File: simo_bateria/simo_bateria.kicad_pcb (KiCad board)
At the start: 2 copper layers, 70 x 163.5 mm, 14 parts, among them J1 BAT_LEVEL, J2 Plugin, SW1 SW_Reed, U1 mod_mt3608, U2 BSS314PEH6327XTSA1

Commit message: revision 3.0. Esquema. PCB con posicionamiento tentativo. Falta ver la posicion definitiva y mas conveniente del switch magnetico
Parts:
- added J3: VBAT IN, simo_bateria:JST_EH_B2B-EH-A_1x02_P2.50mm_Vertical, F.Cu at (160.1, 69.5)
- BT1, BT2: value Battery_Cell -> Bateria; footprint simo_bateria:BatteryHolder_MPD_BH-18650-PC2 -> simo_bateria:BH-18650-PC2_virtual
- R1, R2, R3, SW1: footprint Resistor_THT:R_Axial_DIN0309_L9.0mm_D3.2mm_P25.40mm_Horizontal -> Resistor_THT:R_Axial_DIN0309_L9.0mm_D3.2mm_P15.24mm_Horizontal
- U2: moved to B.Cu
- moved BT1 131.6 mm to (60.5, 61.0), turned to 0 degrees
- moved J1 108.9 mm to (160.9, 76.7)
- moved U1 88.7 mm to (193.1, 64.5)
- moved BT2 49.9 mm to (60.5, 82.5), turned to 0 degrees
- moved R3 45.1 mm to (198.1, 82.0), turned to 180 degrees
- moved H2 40.7 mm to (161.6, 59.5)
- moved H1 40.4 mm to (213.6, 59.5)
- moved U2 31.3 mm to (191.6, 75.5), turned to 180 degrees
- moved SW1 30.1 mm to (183.0, 86.5)
- moved J2 29.1 mm to (212.6, 76.3)
- moved R1 25.9 mm to (175.0, 72.4), turned to -90 degrees
- moved R2 23.2 mm to (170.6, 87.6), turned to 90 degrees
- moved H4 23.2 mm to (161.6, 85.5)
- moved H3 22.7 mm to (213.6, 85.0)
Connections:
- BT1 pad 1: Net-(BT1-Pad1) -> unconnected-(BT1-Pad1)
- BT1 pad 2: Net-(BT1-Pad2) -> unconnected-(BT1-Pad2)
- BT2 pad 1: Net-(BT1-Pad1) -> unconnected-(BT2-Pad1)
- BT2 pad 2: Net-(BT1-Pad2) -> unconnected-(BT2-Pad2)
- J1 pad 1: GND -> Net-(J1-Pad1)
- J2 pad 1: GND -> Net-(J2-Pad1)
- R1 pad 1: Net-(BT1-Pad1) -> Net-(R1-Pad1)
- R2 pad 2: GND -> Net-(J1-Pad1)
- R3 pad 2: Net-(BT1-Pad2) -> Net-(R3-Pad2)
- SW1 pad 1: Net-(BT1-Pad1) -> Net-(R1-Pad1)
- U1 pad 2: Net-(BT1-Pad2) -> Net-(R3-Pad2)
- U1 pad 4: GND -> Net-(J2-Pad1)
- U2 pad 3: Net-(BT1-Pad1) -> Net-(R1-Pad1)
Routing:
- net Net-(R1-Pad1): track 0.00 -> 47.1 mm
- net Net-(R3-Pad2): track 0.00 -> 32.9 mm
- net Net-(J2-Pad2): track 0.00 -> 22.8 mm
- net Net-(U1-Pad1): track 0.00 -> 22.1 mm
- net Net-(J1-Pad2): track 0.00 -> 18.3 mm
- net Net-(R3-Pad1): track 0.00 -> 14.9 mm
- net Net-(J1-Pad1): track 0.00 -> 13.0 mm
- net Net-(J2-Pad1): track 0.00 -> 7.78 mm
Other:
- board size 70 x 163.5 mm -> 65 x 35 mm
- board text added: "Los portabaterias no forman parte del pcb. La tension de entrada ingresa por el conector VBAT IN"
- board text added: "Posicionamiento tentativo. Aun falta definir y probar dorde ira el switch magnetico"

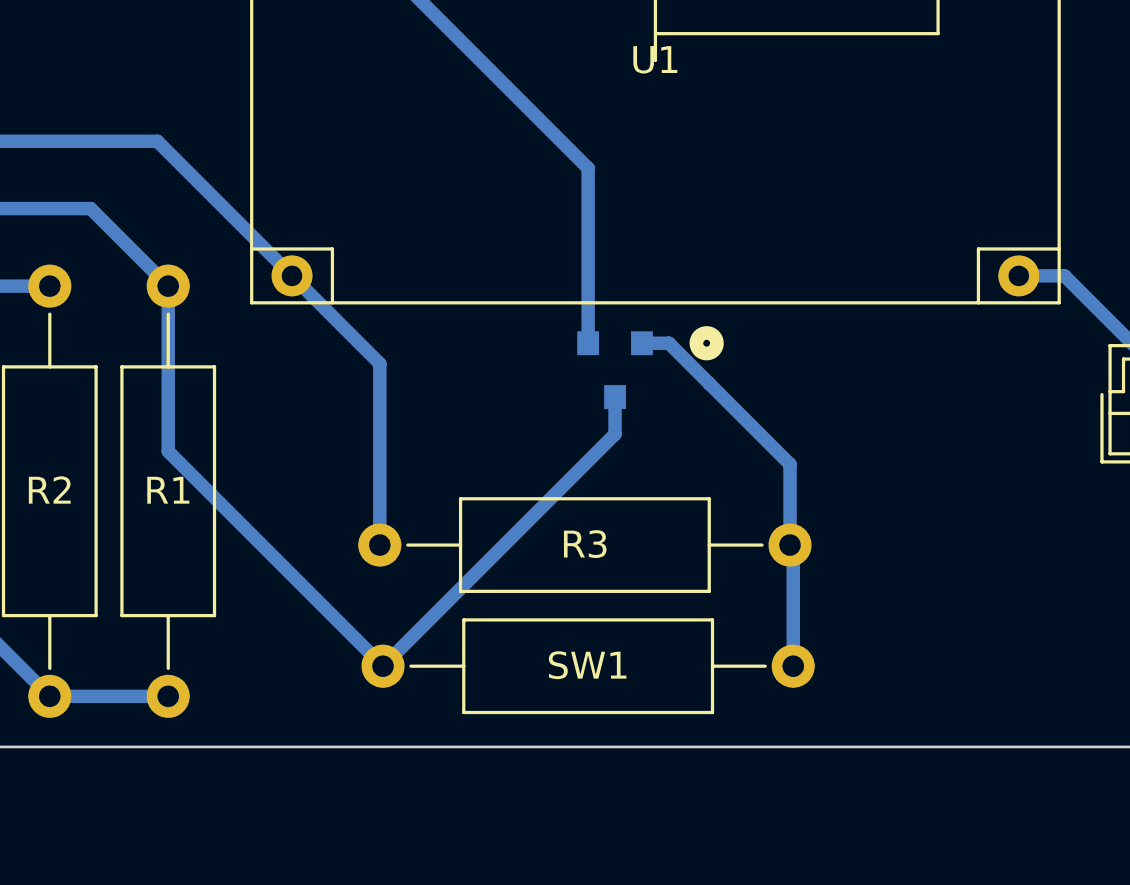
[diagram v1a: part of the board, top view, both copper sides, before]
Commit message: se agrego bornera para el switch magnetico. El pcb tengo 2 warnings a revisar
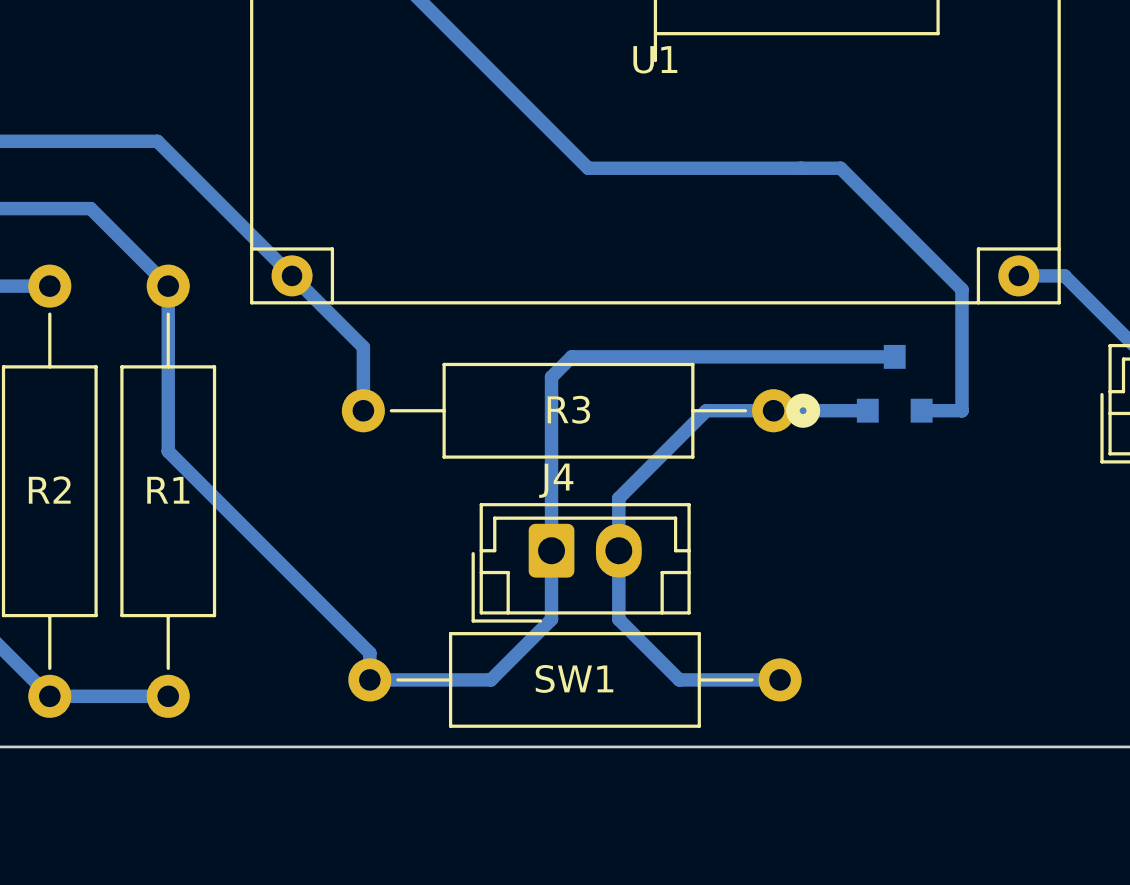
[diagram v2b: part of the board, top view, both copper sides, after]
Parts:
- added J4: SWD, simo_bateria:JST_EH_B2B-EH-A_1x02_P2.50mm_Vertical, F.Cu at (189.2, 82.2)
- moved U2 10.4 mm to (202.0, 76.0), turned to 0 degrees
- moved R3 5.03 mm to (197.5, 77.0)
- moved SW1 0.71 mm to (182.5, 87.0)
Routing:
- net Net-(J3-Pad1): track 47.1 -> 63.6 mm
- net Net-(U1-Pad1): track 22.1 -> 37.3 mm
- net Net-(R3-Pad1): track 14.9 -> 22.0 mm
- net Net-(J3-Pad2): track 32.9 -> 27.7 mm

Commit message: Update
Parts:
- moved R3 23.6 mm to (174.5, 82.5), turned to 90 degrees
- moved R2 20.3 mm to (170.5, 67.3), turned to -90 degrees
- moved SW1 16.5 mm to (166.0, 86.5)
- moved R1 13.2 mm to (166.5, 82.5), turned to 90 degrees
- moved U2 13.0 mm to (189.0, 75.5), turned to 180 degrees
- moved J1 2.41 mm to (158.7, 77.8), turned to 90 degrees
- moved J3 1.59 mm to (158.7, 68.8)
- moved U1 0.89 mm to (194.0, 64.5)
- moved J4 0.39 mm to (189.0, 82.5), turned to -90 degrees
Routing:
- net Net-(U1-Pad1): track 37.3 -> 20.6 mm
- net Net-(J4-Pad2): track 22.0 -> 31.2 mm
- net Net-(J1-Pad2): track 18.3 -> 15.5 mm
- net Net-(J1-Pad1): track 13.0 -> 15.6 mm
- net Net-(J3-Pad2): track 27.7 -> 29.8 mm
- net Net-(J2-Pad1): track 7.78 -> 6.89 mm

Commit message: UPDATE
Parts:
- R1: value 355k -> 10k; footprint Resistor_THT:R_Axial_DIN0309_L9.0mm_D3.2mm_P15.24mm_Horizontal -> simo_bateria:RESITOR_THT
- R2: value 155k -> 355k; footprint Resistor_THT:R_Axial_DIN0309_L9.0mm_D3.2mm_P15.24mm_Horizontal -> simo_bateria:RESITOR_THT
- R3: value 10k -> 155k; footprint Resistor_THT:R_Axial_DIN0309_L9.0mm_D3.2mm_P15.24mm_Horizontal -> simo_bateria:RESITOR_THT
- SW1: footprint Resistor_THT:R_Axial_DIN0309_L9.0mm_D3.2mm_P15.24mm_Horizontal -> simo_bateria:RESITOR_THT
- moved U2 58.8 mm to (179.1, 133.5), turned to 90 degrees
- moved J4 58.0 mm to (172.0, 138.0), turned to 0 degrees
- moved R1 56.7 mm to (199.0, 129.0), turned to 180 degrees
- moved J2 53.7 mm to (213.0, 130.0)
- moved U1 53.5 mm to (195.0, 118.0)
- moved H1 52.5 mm to (215.0, 112.0)
- moved H2 52.5 mm to (161.0, 112.0)
- moved J1 52.3 mm to (160.0, 130.0)
- moved J3 52.3 mm to (160.0, 121.0)
- moved H3 52.0 mm to (215.0, 137.0)
- moved H4 51.5 mm to (161.0, 137.0)
- moved SW1 51.5 mm to (166.0, 138.0)
- moved R2 45.7 mm to (172.0, 113.0)
- moved R3 31.4 mm to (167.0, 113.0), turned to -90 degrees
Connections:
- R1 pad 1: Net-(J3-Pad1) -> Net-(J4-Pad2)
- R1 pad 2: Net-(J1-Pad2) -> Net-(J3-Pad2)
- R2 pad 2: Net-(J1-Pad1) -> Net-(J3-Pad1)
- R3 pad 1: Net-(J4-Pad2) -> Net-(J1-Pad2)
- R3 pad 2: Net-(J3-Pad2) -> Net-(J1-Pad1)
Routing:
- net Net-(J3-Pad1): track 64.1 -> 36.0 mm
- net Net-(J1-Pad2): track 15.5 -> 28.4 mm
- net Net-(U1-Pad1): track 20.6 -> 28.6 mm
- net Net-(J4-Pad2): track 31.2 -> 37.7 mm
- net Net-(J1-Pad1): track 15.6 -> 10.7 mm
- net Net-(J2-Pad1): track 6.89 -> 8.12 mm
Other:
- board size 65 x 35 mm -> 66 x 35 mm

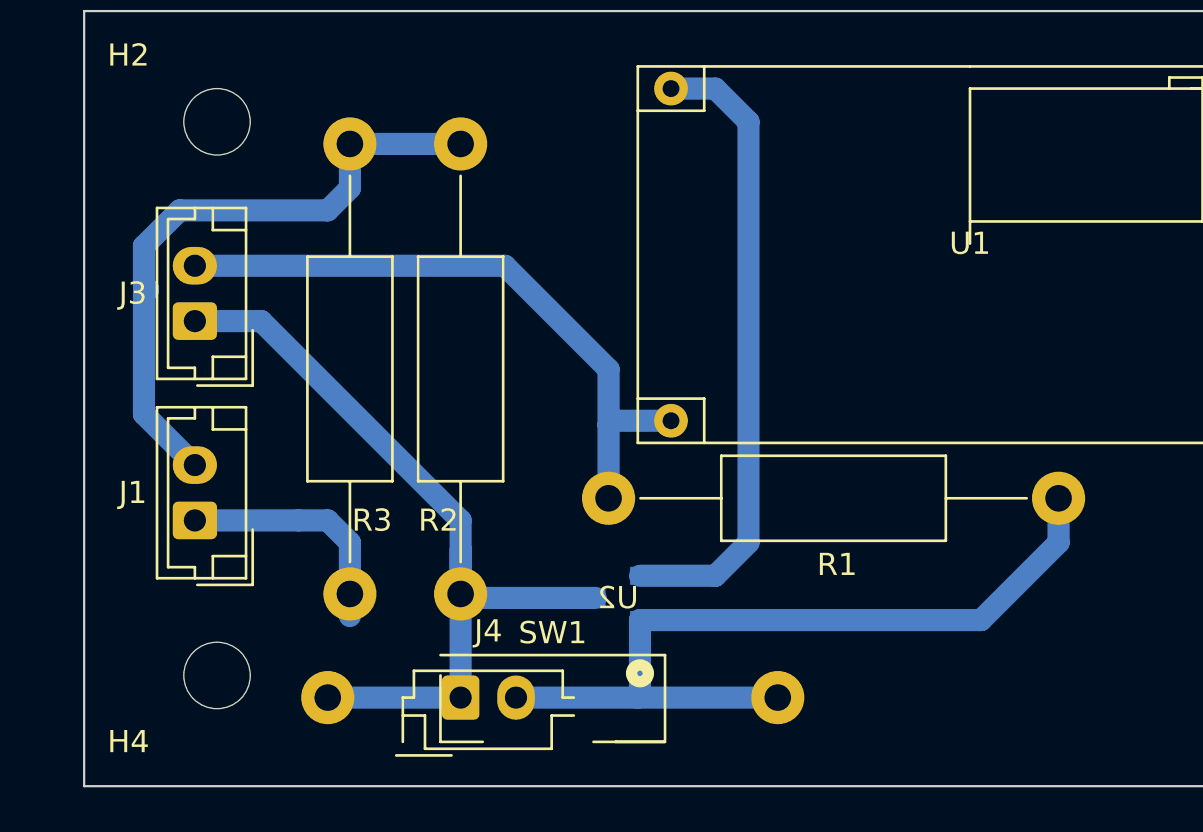
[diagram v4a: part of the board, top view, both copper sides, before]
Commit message: Se efectuaron los siguientes cambios:   - Corrección pista frente a conector J3.   - Modificación de pista entre SW y R1.
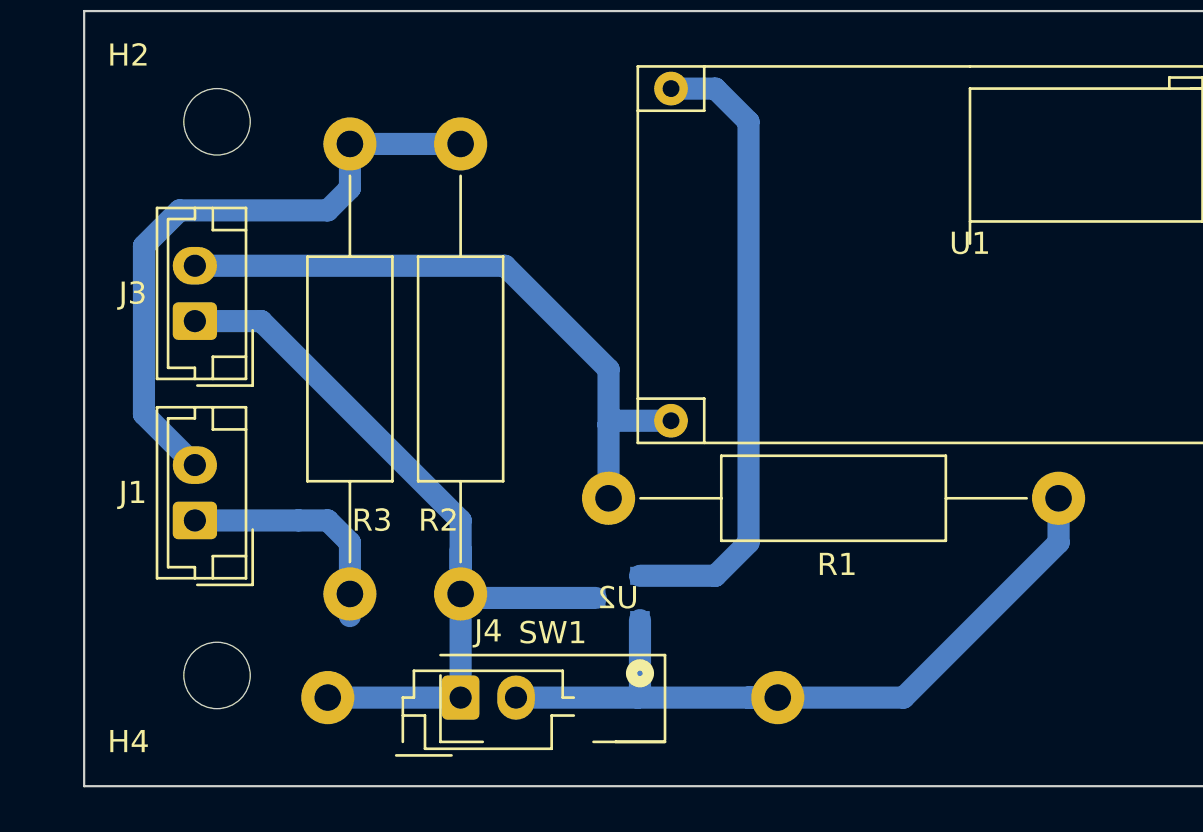
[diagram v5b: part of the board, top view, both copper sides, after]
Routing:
- net Net-(J4-Pad2): track 37.7 -> 34.3 mm
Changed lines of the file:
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@@
     (style (thickness 0.1) (arrow_length 1.27) (text_position_mode 0) (extension_height 0.58642) (extension_offset 0.5) keep_text_aligned)
   )
-  (segment (start 159.309441 116) (end 157.7 117.609441) (width 1) (layer "B.Cu") (net 1))
-  (segment (start 167 115) (end 166 116) (width 1) (layer "B.Cu") (net 1))
+  (segment (start 166 116) (end 167 115) (width 1) (layer "B.Cu") (net 1))
+  (segment (start 157.7 117.609441) (end 159.309441 116) (width 1) (layer "B.Cu") (net 1))
   (segment (start 172 113) (end 167 113) (width 1) (layer "B.Cu") (net 1))
-  (segment (start 157.7 119.390559) (end 157.883705 119.574264) (width 1) (layer "B.Cu") (net 1))
-  (segment (start 157.7 125.2) (end 160 127.5) (width 1) (layer "B.Cu") (net 1))
-  (segment (start 157.7 119.757969) (end 157.7 125.2) (width 1) (layer "B.Cu") (net 1))
-  (segment (start 157.7 117.609441) (end 157.7 119.390559) (width 1) (layer "B.Cu") (net 1))
-  (segment (start 167 113) (end 167 115) (width 1) (layer "B.Cu") (net 1))
-  (segment (start 157.883705 119.574264) (end 157.7 119.757969) (width 1) (layer "B.Cu") (net 1))
-  (segment (start 166 116) (end 159.309441 116) (width 1) (layer "B.Cu") (net 1))
+  (segment (start 157.7 125.2) (end 157.7 117.609441) (width 1) (layer "B.Cu") (net 1))
+  (segment (start 159.309441 116) (end 166 116) (width 1) (layer "B.Cu") (net 1))
+  (segment (start 160 127.5) (end 157.7 125.2) (width 1) (layer "B.Cu") (net 1))
+  (segment (start 167 115) (end 167 113) (width 1) (layer "B.Cu") (net 1))
   (segment (start 208.5 114) (end 215.5 121) (width 1) (layer "B.Cu") (net 5))
   (segment (start 208.5 110.5) (end 208.5 114) (width 1) (layer "B.Cu") (net 5))
@@
   (segment (start 178.68 125.68) (end 178.68 129) (width 1) (layer "B.Cu") (net 11))
   (segment (start 178.86 125.5) (end 178.68 125.68) (width 1) (layer "B.Cu") (net 11))
+  (segment (start 185 138) (end 192 138) (width 1) (layer "B.Cu") (net 12))
+  (segment (start 180 138) (end 185 138) (width 1) (layer "B.Cu") (net 12))
+  (segment (start 185 138) (end 186.32 138) (width 1) (layer "B.Cu") (net 12))
   (segment (start 199 131) (end 199 129) (width 1) (layer "B.Cu") (net 12))
-  (segment (start 180.0983 134.500001) (end 195.499999 134.500001) (width 1) (layer "B.Cu") (net 12))
-  (segment (start 195.499999 134.500001) (end 199 131) (width 1) (layer "B.Cu") (net 12))
   (segment (start 180.0983 137.9017) (end 180 138) (width 1) (layer "B.Cu") (net 12))
+  (segment (start 192 138) (end 199 131) (width 1) (layer "B.Cu") (net 12))
   (segment (start 174.5 138) (end 180 138) (width 1) (layer "B.Cu") (net 12))
-  (segment (start 180 138) (end 186.32 138) (width 1) (layer "B.Cu") (net 12))
   (segment (start 180.0983 134.500001) (end 180.0983 137.9017) (width 1) (layer "B.Cu") (net 12))
 )

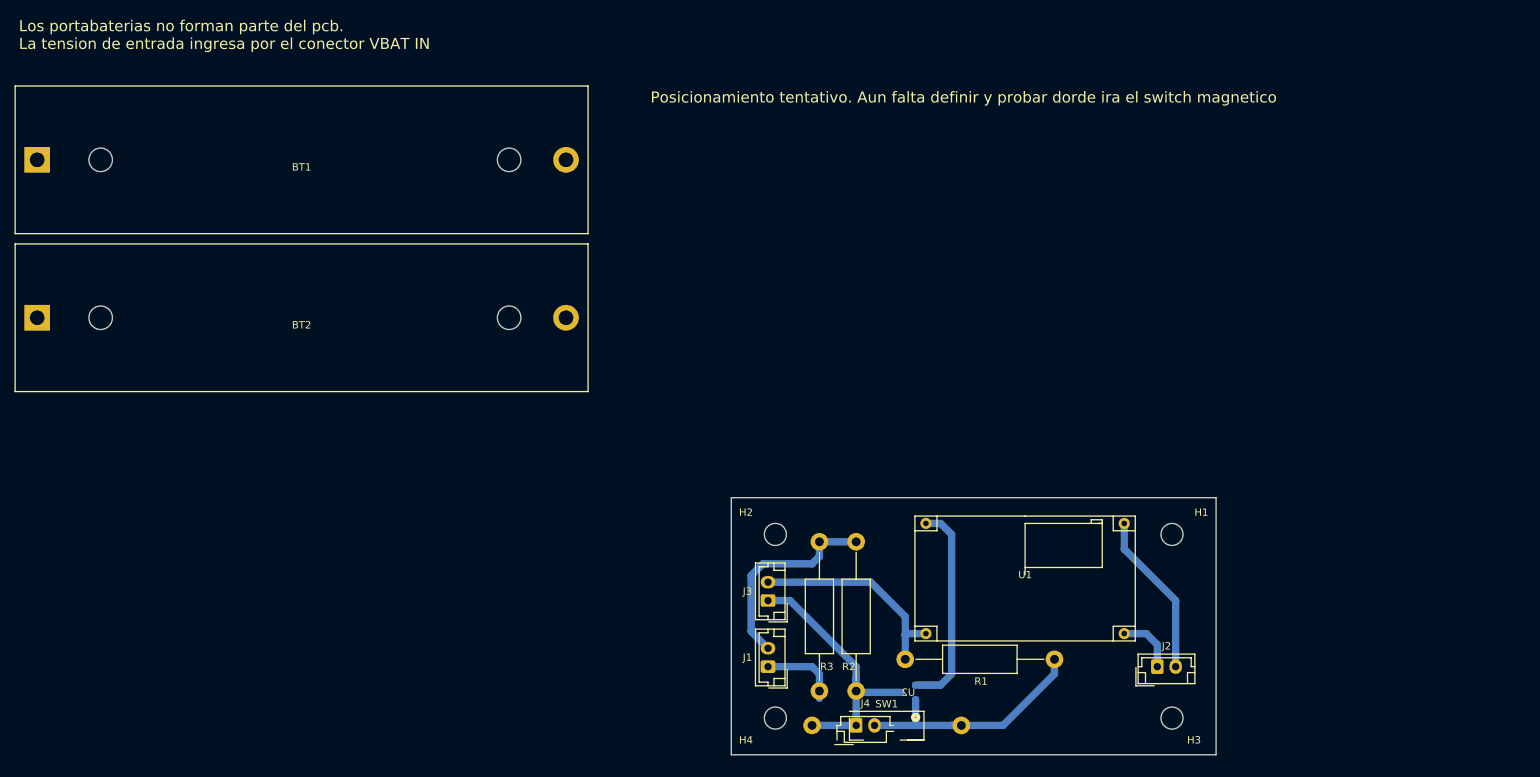
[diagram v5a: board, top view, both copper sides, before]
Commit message: [Modificaciones] Reduccion de PCB para fabricar con CNC
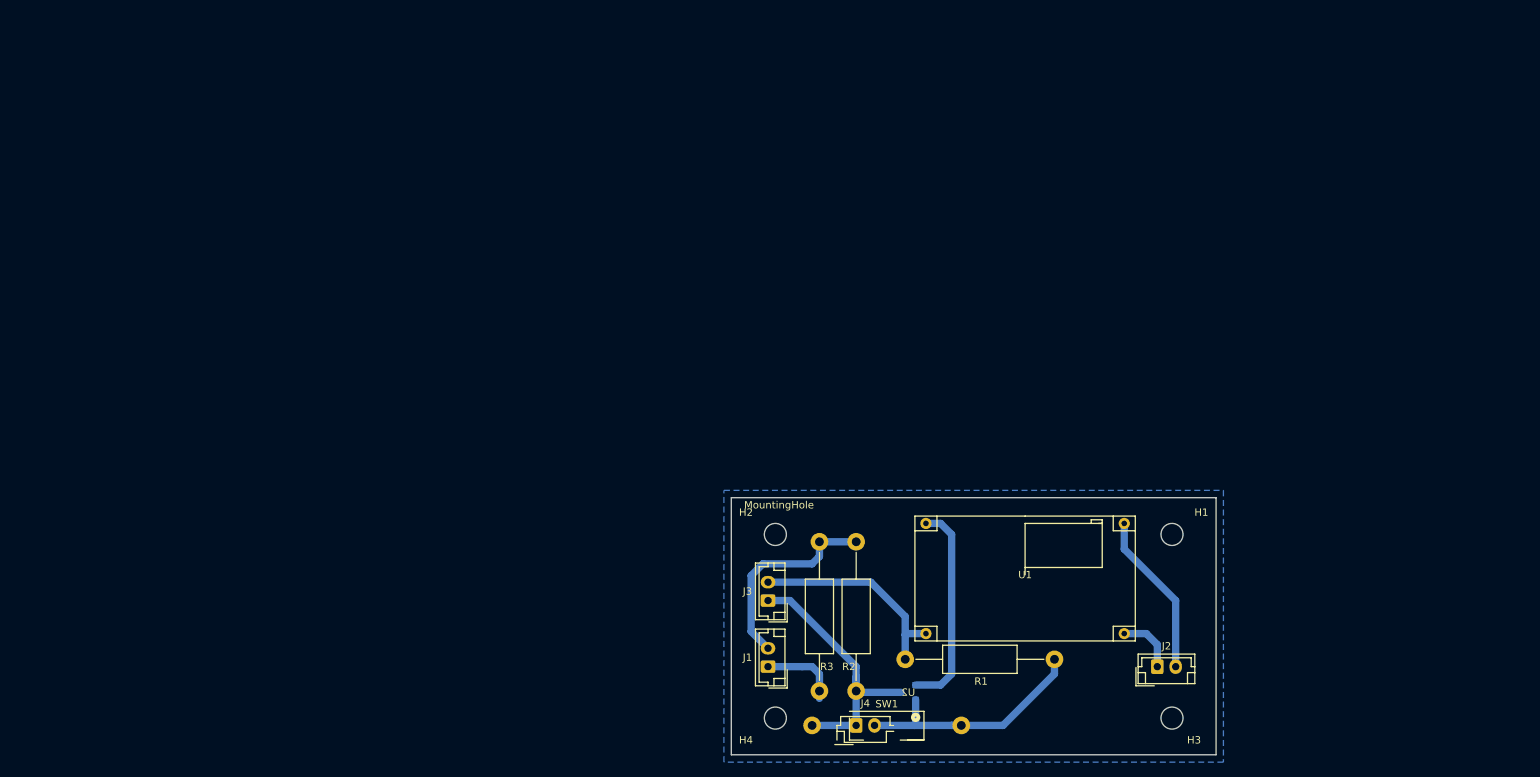
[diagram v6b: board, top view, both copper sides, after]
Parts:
- removed BT1, BT2: Bateria, simo_bateria:BH-18650-PC2_virtual
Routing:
- added copper zone on B.Cu, net (none)
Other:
- board text removed: "Los portabaterias no forman parte del pcb. La tension de entrada ingresa por el conector VBAT IN"
- board text removed: "Posicionamiento tentativo. Aun falta definir y probar dorde ira el switch magnetico"
